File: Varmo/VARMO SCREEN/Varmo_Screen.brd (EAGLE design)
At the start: 160 x 100 mm, 34 parts, among them T1 MMBT2222AL, U1 LT1813CS8, U5 90814-0210

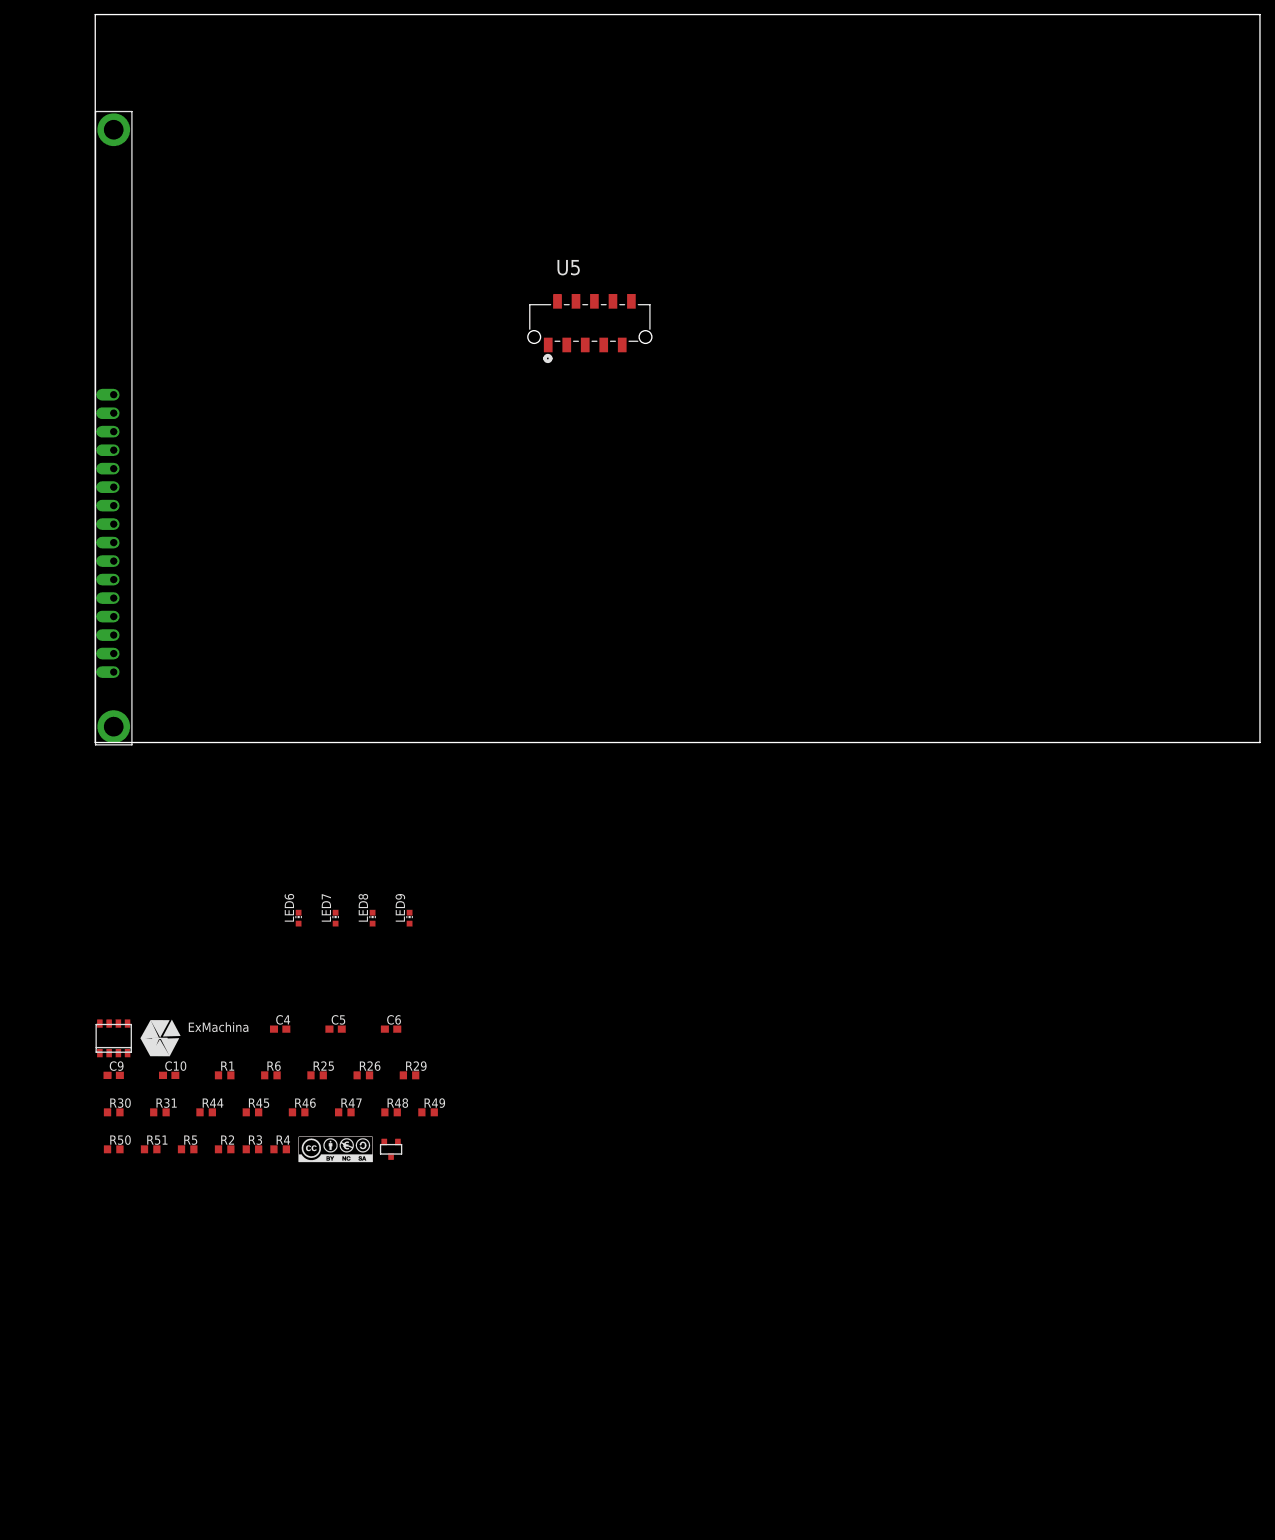
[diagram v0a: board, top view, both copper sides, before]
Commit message: Add PCA9670 to the schematic
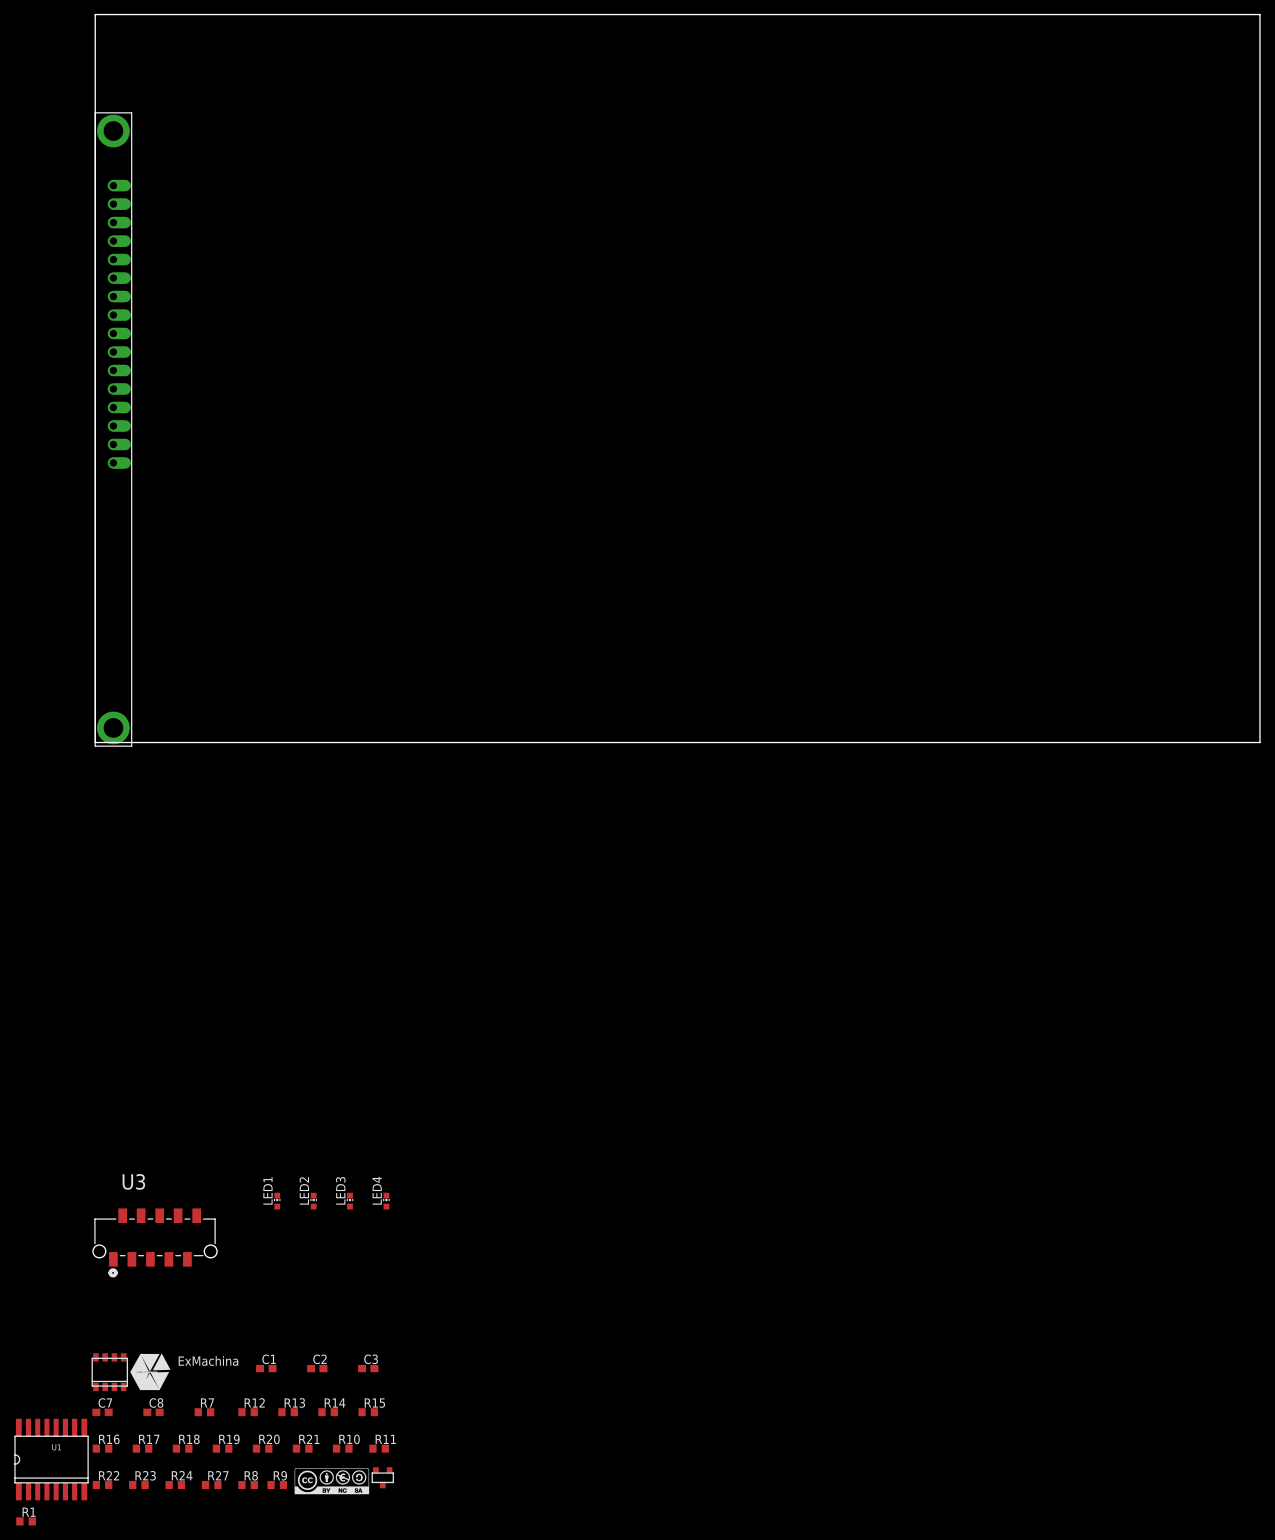
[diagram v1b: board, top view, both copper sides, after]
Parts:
- removed C10, C4, C6, C9: 0.1uF, rcl:C0603
- removed C5: 4.7uF, rcl:C0603
- removed LCD1: MC41605A12W, midas:CONNECTOR
- removed LED6, LED7, LED8, LED9: Blue, led:CHIP-LED0603
- removed R2, R3, R4, R48, R49, R50, R51: 1k, rcl:R0603
- removed R25, R26, R29, R30, R31, R44, R45, R46, R47, R6: 4.7k, rcl:R0603
- removed R5: 10k, rcl:R0603
- removed T1: MMBT2222AL, transistor:SOT−23
- removed U$5: CC-BY-NC-SA, cc-by-sa:CC-BY-NC-SA
- removed U$7: EXMACHINA-LOGO-NAME, exmachina:EXM-LOGO-BASELINE
- removed U5: 90814-0210, Molex_By_element14_Batch_1:MOLEX_90814-0210
- added C1, C3, C7, C8: 0.1uF, rcl:C0603
- added C2: 4.7uF, rcl:C0603
- added LCD2: MC41605A12W, midas:CONNECTOR
- added LED1, LED2, LED3, LED4: Blue, led:CHIP-LED0603
- added R10, R22, R23, R24, R27, R8, R9: 1k, rcl:R0603
- added R11: 10k, rcl:R0603
- added R12, R13, R14, R15, R16, R17, R18, R19, R20, R21: 4.7k, rcl:R0603
- added R7: 100R, rcl:R0603
- added T2: MMBT2222AL, transistor:SOT−23
- added U$1: CC-BY-NC-SA, cc-by-sa:CC-BY-NC-SA
- added U$2: EXMACHINA-LOGO-NAME, exmachina:EXM-LOGO-BASELINE
- added U2: LT1813CS8, lineartechnology:SOIC8
- added U3: 90814-0210, Molex_By_element14_Batch_1:MOLEX_90814-0210
- R1: value 100R -> 4.7k
- U1: value LT1813CS8 -> PCA9670D; device lineartechnology:SOIC8 -> NXP:SOT162-1
- moved R1 67.1 mm to (-9.50, -107.0)
- moved U1 58.5 mm to (-6.00, -98.5)
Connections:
- removed net N$14: R3.1, R4.2, U1.6
- removed net N$17: R4.1, R5.2, U1.7
- removed net N$2: C4.1, R1.2, T1.1
- removed net N$22: LED7.A, R49.1
- removed net N$24: LED8.A, R50.1
- removed net N$29: LED9.A, R51.1
- removed net N$3: R2.1, T1.3, U1.3
- removed net N$4: LED6.A, R48.1
- removed net N$5: R3.2, U1.1, U1.2
- new net N$1: C1.1, R7.2, T2.1
- new net N$10: LED1.A, R22.1
- new net N$11: LED2.A, R23.1
- new net N$12: LED3.A, R24.1
- new net N$13: LED4.A, R27.1
- new net N$6: R8.1, T2.3, U2.3
- new net N$7: R9.2, U2.1, U2.2
- new net N$8: R10.2, R9.1, U2.6
- new net N$9: R10.1, R11.2, U2.7
- new net RESET: R1.1, U1.13
- net +3V3: now also C8.1, R1.2, R20.2, R21.2, U1.16, U3.2; no longer C9.1, R46.2, R47.2, U5.2
- net +5V/1: now also C3.1, LCD2.2, LCD2.4, LCD2.6, R12.2, R13.2, R14.2, R15.2, R16.2, R17.2, R18.2, R19.2, R8.2, U2.8, U3.1; no longer C6.1, LCD1.2, LCD1.4, LCD1.6, R2.2, R25.2, R26.2, R29.2, R30.2, R31.2, R44.2, R45.2, R6.2, U1.8, U5.1
- net D0: now also LCD2.7, R12.1, U1.4; no longer LCD1.7, R6.1
- net D1: now also LCD2.8, R13.1, U1.5; no longer LCD1.8, R25.1
- net D2: now also LCD2.9, R14.1, U1.6; no longer LCD1.9, R26.1
- net D3: now also LCD2.10, R15.1, U1.7; no longer LCD1.10, R29.1
- net D4: now also LCD2.11, R16.1, U1.9; no longer LCD1.11, R30.1
- net D5: now also LCD2.12, R17.1, U1.10; no longer LCD1.12, R31.1
- net D6: now also LCD2.13, R18.1, U1.11; no longer LCD1.13, R44.1
- net D7: now also LCD2.14, R19.1, U1.12; no longer LCD1.14, R45.1
- net GND1: now also C1.2, C2.2, C3.2, C7.2, C8.2, LCD2.1, LCD2.16, LCD2.5, LED1.C, LED2.C, LED3.C, LED4.C, T2.2, U1.1, U1.2, U1.8, U2.5, U3.7; no longer C10.2, C4.2, C5.2, C6.2, C9.2, LCD1.1, LCD1.16, LCD1.5, LED6.C, LED7.C, LED8.C, LED9.C, T1.2, U1.5, U5.7
- net LED_STATUS_1: now also R22.2, U3.10; no longer R48.2, U5.10
- net LED_STATUS_2: now also R23.2, U3.8; no longer R49.2, U5.8
- net LED_STATUS_3: now also R24.2, U3.6; no longer R50.2, U5.6
- net LED_STATUS_4: now also R27.2, U3.4; no longer R51.2, U5.4
- net PWM_CONTRASTE: now also R7.1, U3.9; no longer R1.1, U5.9
- net SCL: now also R21.1, U1.14, U3.5; no longer R47.1, U5.5
- net SDA: now also R20.1, U1.15, U3.3; no longer R46.1, U5.3
- net VEE: now also C7.1, LCD2.15, U2.4; no longer C10.1, LCD1.15, U1.4
- net VO: now also C2.1, LCD2.3, R11.1; no longer C5.1, LCD1.3, R5.1

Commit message: Re routing the board
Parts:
- removed C1, C3, C7, C8: 0.1uF, rcl:C0603
- removed C2: 4.7uF, rcl:C0603
- removed LCD2: MC41605A12W, midas:CONNECTOR
- removed LED1, LED2, LED3, LED4: Blue, led:CHIP-LED0603
- removed R10, R22, R23, R24, R27, R8, R9: 1k, rcl:R0603
- removed R11: 10k, rcl:R0603
- removed R12, R13, R14, R15, R16, R17, R18, R19, R20, R21: 4.7k, rcl:R0603
- removed T2: MMBT2222AL, transistor:SOT−23
- removed U$1: CC-BY-NC-SA, cc-by-sa:CC-BY-NC-SA
- removed U$2: EXMACHINA-LOGO-NAME, exmachina:EXM-LOGO-BASELINE
- removed U3: 90814-0210, Molex_By_element14_Batch_1:MOLEX_90814-0210
- added C10, C4, C6, C9: 0.1uF, rcl:C0603
- added C5: 4.7uF, rcl:C0603
- added LCD1: MC41605A12W, midas:CONNECTOR
- added LED6, LED7, LED8, LED9: Blue, led:CHIP-LED0603
- added R2, R3, R4, R48, R49, R50, R51: 1k, rcl:R0603
- added R25, R26, R29, R30, R31, R44, R45, R46, R47, R6: 4.7k, rcl:R0603
- added R5: 10k, rcl:R0603
- added T1: MMBT2222AL, transistor:SOT−23
- added U$5: CC-BY-NC-SA, cc-by-sa:CC-BY-NC-SA
- added U$7: EXMACHINA-LOGO-NAME, exmachina:EXM-LOGO-BASELINE
- added U5: 90814-0210, Molex_By_element14_Batch_1:MOLEX_90814-0210
- R1: value 4.7k -> 100R
- R7: value 100R -> 4.7k
- U1: value PCA9670D -> LT1813CS8; device NXP:SOT162-1 -> lineartechnology:SOIC8
- U2: value LT1813CS8 -> PCA9670D; device lineartechnology:SOIC8 -> NXP:SOT162-1
- moved R1 180.1 mm to (48.8, 63.5), flipped to the bottom
- moved U1 179.4 mm to (47.4, 72.7), flipped to the bottom
- moved R7 173.6 mm to (21.3, 81.5), turned to 90 degrees
- moved U2 162.7 mm to (9.50, 76.0), turned to 270 degrees
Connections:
- removed net N$10: LED1.A, R22.1
- removed net N$11: LED2.A, R23.1
- removed net N$12: LED3.A, R24.1
- removed net N$13: LED4.A, R27.1
- removed net N$6: R8.1, T2.3, U2.3
- removed net N$7: R9.2, U2.1, U2.2
- removed net N$8: R10.2, R9.1, U2.6
- removed net N$9: R10.1, R11.2, U2.7
- removed net RESET: R1.1, U1.13
- new net N$14: R3.1, R4.2, U1.6
- new net N$17: R4.1, R5.2, U1.7
- new net N$2: C4.1, R1.2, T1.1
- new net N$22: LED7.A, R49.1
- new net N$24: LED8.A, R50.1
- new net N$29: LED9.A, R51.1
- new net N$3: R2.1, T1.3, U1.3
- new net N$4: LED6.A, R48.1
- new net N$5: R3.2, U1.1, U1.2
- net +3V3: now also C9.1, R46.2, R47.2, R7.2, U2.16, U5.2; no longer C8.1, R1.2, R20.2, R21.2, U1.16, U3.2
- net +5V/1: now also C6.1, LCD1.2, LCD1.4, LCD1.6, R2.2, R25.2, R26.2, R29.2, R30.2, R31.2, R44.2, R45.2, R6.2, U1.8, U5.1; no longer C3.1, LCD2.2, LCD2.4, LCD2.6, R12.2, R13.2, R14.2, R15.2, R16.2, R17.2, R18.2, R19.2, R8.2, U2.8, U3.1
- net D0: now also LCD1.7, R6.1, U2.4; no longer LCD2.7, R12.1, U1.4
- net D1: now also LCD1.8, R25.1, U2.5; no longer LCD2.8, R13.1, U1.5
- net D2: now also LCD1.9, R26.1, U2.6; no longer LCD2.9, R14.1, U1.6
- net D3: now also LCD1.10, R29.1, U2.7; no longer LCD2.10, R15.1, U1.7
- net D4: now also LCD1.11, R30.1, U2.9; no longer LCD2.11, R16.1, U1.9
- net D5: now also LCD1.12, R31.1, U2.10; no longer LCD2.12, R17.1, U1.10
- net D6: now also LCD1.13, R44.1, U2.11; no longer LCD2.13, R18.1, U1.11
- net D7: now also LCD1.14, R45.1, U2.12; no longer LCD2.14, R19.1, U1.12
- net GND1: now also C10.2, C4.2, C5.2, C6.2, C9.2, LCD1.1, LCD1.16, LCD1.5, LED6.C, LED7.C, LED8.C, LED9.C, T1.2, U1.5, U2.1, U2.2, U2.3, U2.8, U5.7; no longer C1.2, C2.2, C3.2, C7.2, C8.2, LCD2.1, LCD2.16, LCD2.5, LED1.C, LED2.C, LED3.C, LED4.C, T2.2, U1.1, U1.2, U1.8, U2.5, U3.7
- net LED_STATUS_1: now also R48.2, U5.10; no longer R22.2, U3.10
- net LED_STATUS_2: now also R49.2, U5.8; no longer R23.2, U3.8
- net LED_STATUS_3: now also R50.2, U5.6; no longer R24.2, U3.6
- net LED_STATUS_4: now also R51.2, U5.4; no longer R27.2, U3.4
- net N$1: now also R7.1, U2.13; no longer C1.1, R7.2, T2.1
- net PWM_CONTRASTE: now also R1.1, U5.9; no longer R7.1, U3.9
- net SCL: now also R47.1, U2.14, U5.5; no longer R21.1, U1.14, U3.5
- net SDA: now also R46.1, U2.15, U5.3; no longer R20.1, U1.15, U3.3
- net VEE: now also C10.1, LCD1.15, U1.4; no longer C7.1, LCD2.15, U2.4
- net VO: now also C5.1, LCD1.3, R5.1; no longer C2.1, LCD2.3, R11.1
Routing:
- net SDA: track 0.00 -> 100.9 mm, vias 0 -> 3
- net SCL: track 0.00 -> 96.9 mm, vias 0 -> 2
- net D7: track 0.00 -> 53.2 mm, vias 0 -> 2
- net LED_STATUS_1: track 0.00 -> 51.1 mm, vias 0 -> 1
- net D6: track 0.00 -> 50.8 mm, vias 0 -> 2
- net D5: track 0.00 -> 48.1 mm, vias 0 -> 2
- net D4: track 0.00 -> 45.3 mm, vias 0 -> 2
- net D3: track 0.00 -> 41.7 mm, vias 0 -> 2
- net LED_STATUS_2: track 0.00 -> 38.9 mm, vias 0 -> 1
- net D2: track 0.00 -> 35.8 mm, vias 0 -> 2
- net D1: track 0.00 -> 29.5 mm, vias 0 -> 2
- net LED_STATUS_3: track 0.00 -> 25.9 mm, vias 0 -> 1
- net D0: track 0.00 -> 24.7 mm, vias 0 -> 2
- net PWM_CONTRASTE: track 0.00 -> 22.8 mm, vias 0 -> 2
- net VEE: track 0.00 -> 21.4 mm
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- added copper zone on layer 1, net +3V3
- added copper zone on layer 16, net +3V3
- added copper zone on layer 1, net +5V/1
- added copper zone on layer 16, net GND1
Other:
- board size 160 x 100 mm -> 40 x 98 mm
- board text added: "Varmo Rev A2"

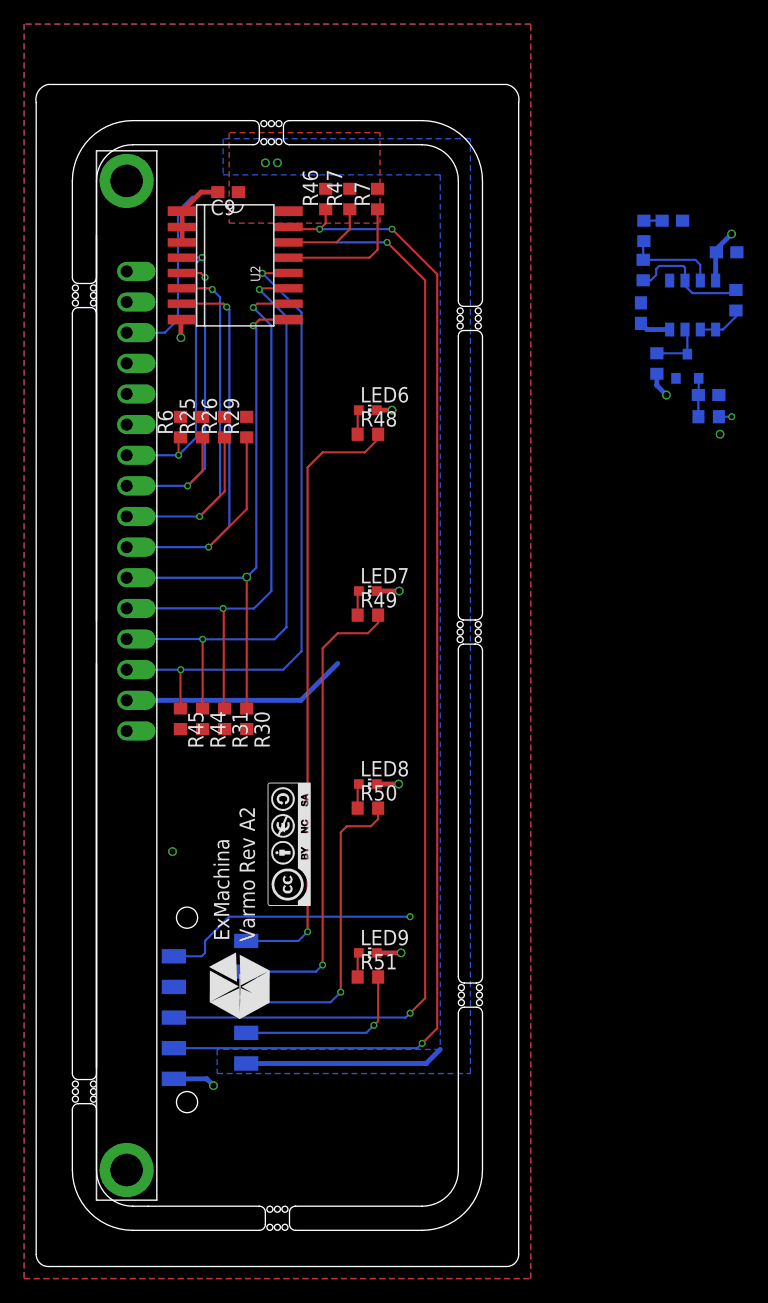
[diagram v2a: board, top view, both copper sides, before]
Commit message: Update the LT1813 devide
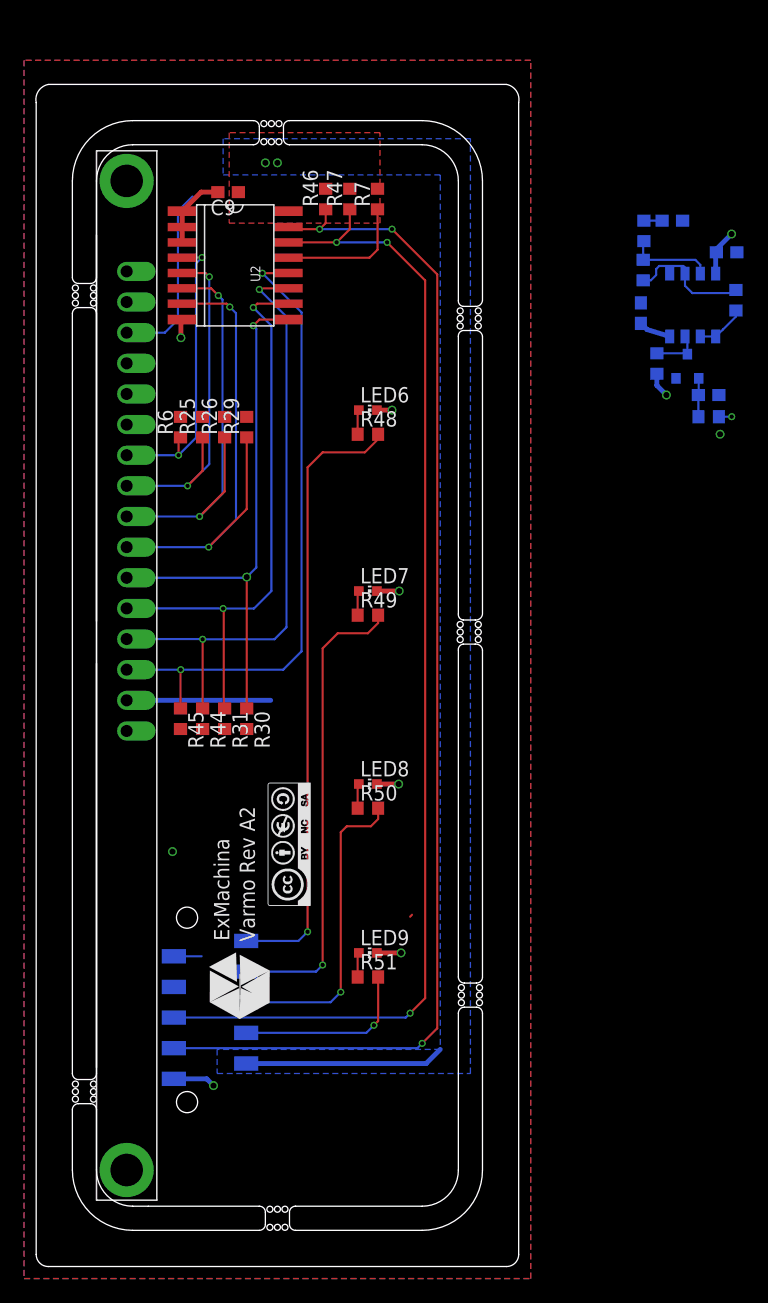
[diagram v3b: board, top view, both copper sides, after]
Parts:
- U1: value LT1813CS8 -> LT1813; device lineartechnology:SOIC8 -> lineartechnology:S8
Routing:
- net PWM_CONTRASTE: track 22.8 -> 3.59 mm, vias 2 -> 1
- net VEE: track 21.4 -> 14.6 mm
- net D3: track 41.7 -> 42.3 mm
- net N$17: track 7.78 -> 7.21 mm
- net +5V/1: track 10.0 -> 9.44 mm
- net D1: track 29.5 -> 30.0 mm
- net SCL: vias 2 -> 3
